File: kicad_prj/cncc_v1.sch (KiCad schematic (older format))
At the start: 0 parts

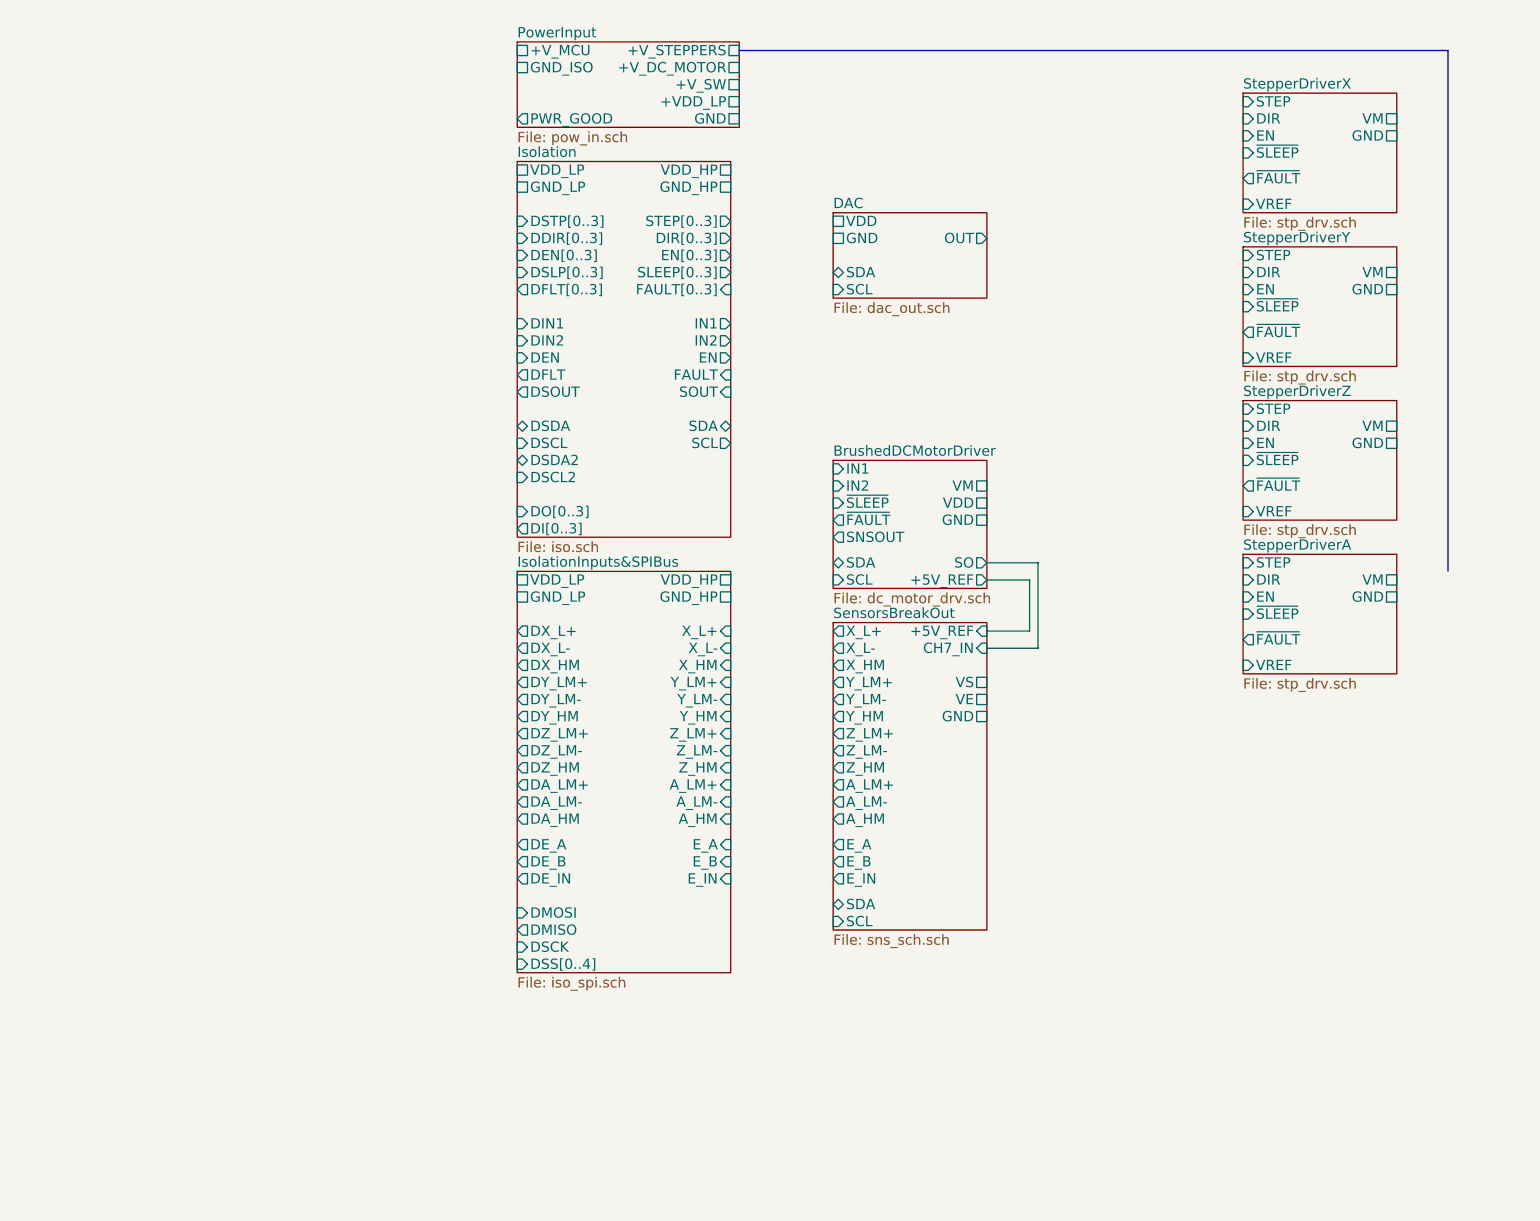
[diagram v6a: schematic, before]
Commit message: Schematics 10
All power isolated part is wired.
Started control part.
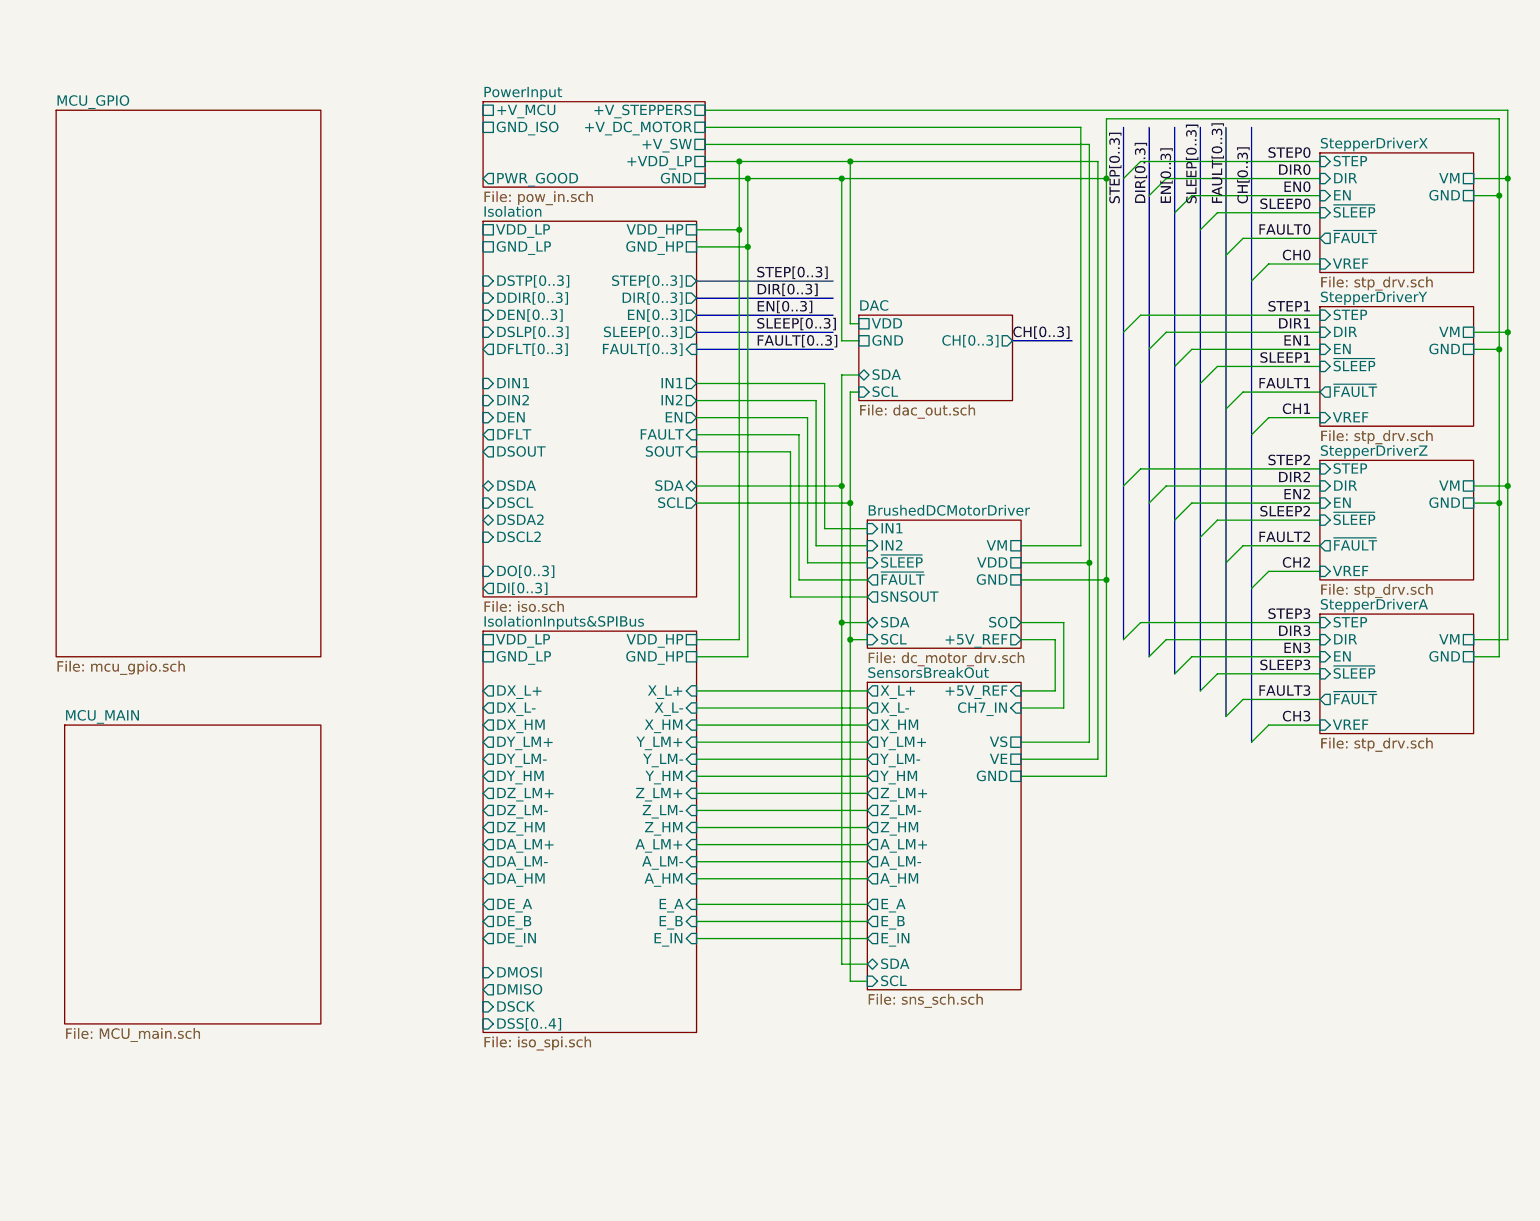
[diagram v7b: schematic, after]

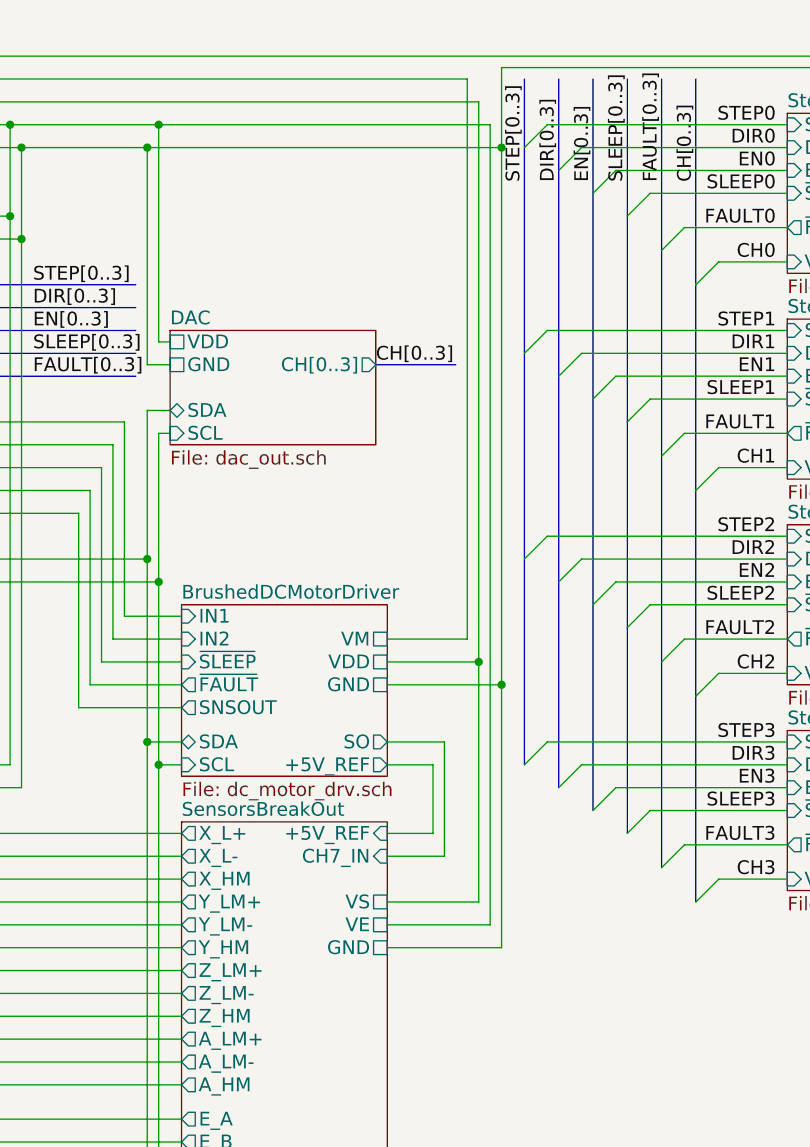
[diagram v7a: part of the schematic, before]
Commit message: Buffers for limit switches
Added buffers and filters.
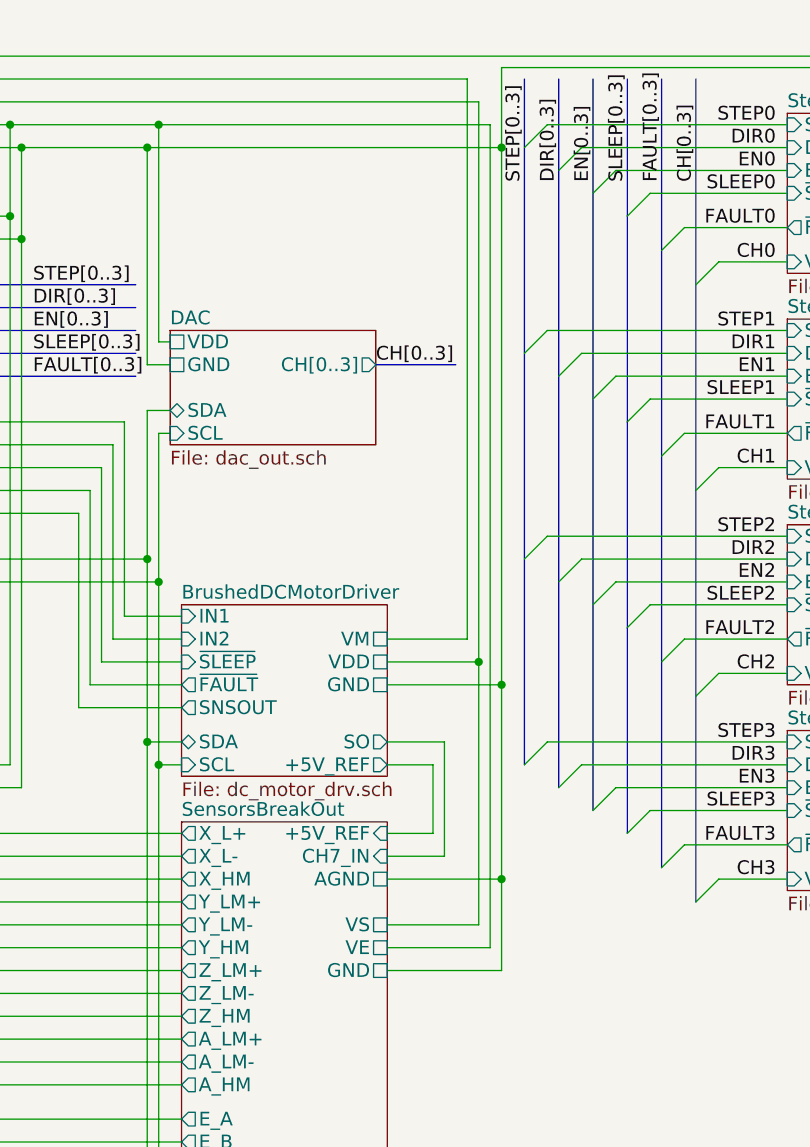
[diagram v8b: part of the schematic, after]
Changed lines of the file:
@@
 F0 "SensorsBreakOut" 60
 F1 "sns_sch.sch" 60
-F2 "VS" U R 7400 4800 60
-F3 "VE" U R 7400 4900 60
-F4 "GND" U R 7400 5000 60
+F2 "VS" U R 7400 4900 60
+F3 "VE" U R 7400 5000 60
+F4 "GND" U R 7400 5100 60
 F5 "X_L+" O L 6500 4500 60
 F6 "X_L-" O L 6500 4600 60
@@
 F22 "SCL" I L 6500 6200 60
 F23 "CH7_IN" I R 7400 4600 60
+F24 "AGND" U R 7400 4700 60
 $EndSheet
 $Sheet
@@
 	5550 1300 7800 1300
 Wire Wire Line
-	7800 1300 7800 4800
-Wire Wire Line
-	7800 4800 7400 4800
+	7800 1300 7800 4900
 Wire Wire Line
 	7400 3750 7800 3750
@@
 	5550 1400 7850 1400
 Wire Wire Line
-	7850 1400 7850 4900
-Wire Wire Line
-	7850 4900 7400 4900
+	7850 1400 7850 5000
 Wire Wire Line
 	6400 1400 6400 2350
@@
 	5550 1500 7900 1500
 Wire Wire Line
-	7900 1150 7900 5000
-Wire Wire Line
-	7900 5000 7400 5000
+	7900 1150 7900 5100
 Wire Wire Line
 	7400 3850 7900 3850
@@
 F1 "MCU_main.sch" 60
 $EndSheet
+Wire Wire Line
+	7900 5100 7400 5100
+Wire Wire Line
+	7850 5000 7400 5000
+Wire Wire Line
+	7800 4900 7400 4900
+Wire Wire Line
+	7400 4700 7900 4700
+Connection ~ 7900 4700
 $EndSCHEMATC
